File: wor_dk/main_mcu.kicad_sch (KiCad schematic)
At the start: 54 parts, among them J201 USB_A, J202 Prog, J203 u.FL, SW201 SW_Push, SW202 SW_Push, U201 nRF52840, Y201 32MHz, Y202 32.768kHz

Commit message: wor_dk: add top-level hierarchical sheets & update annotation
- import hierarchical sheet for main MCU
- import hierarchical sheet for transceiver MCU
- import hierarchical sheet for controller MCU
- update annotations for controller MCU
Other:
- title: MCU -> Main MCU

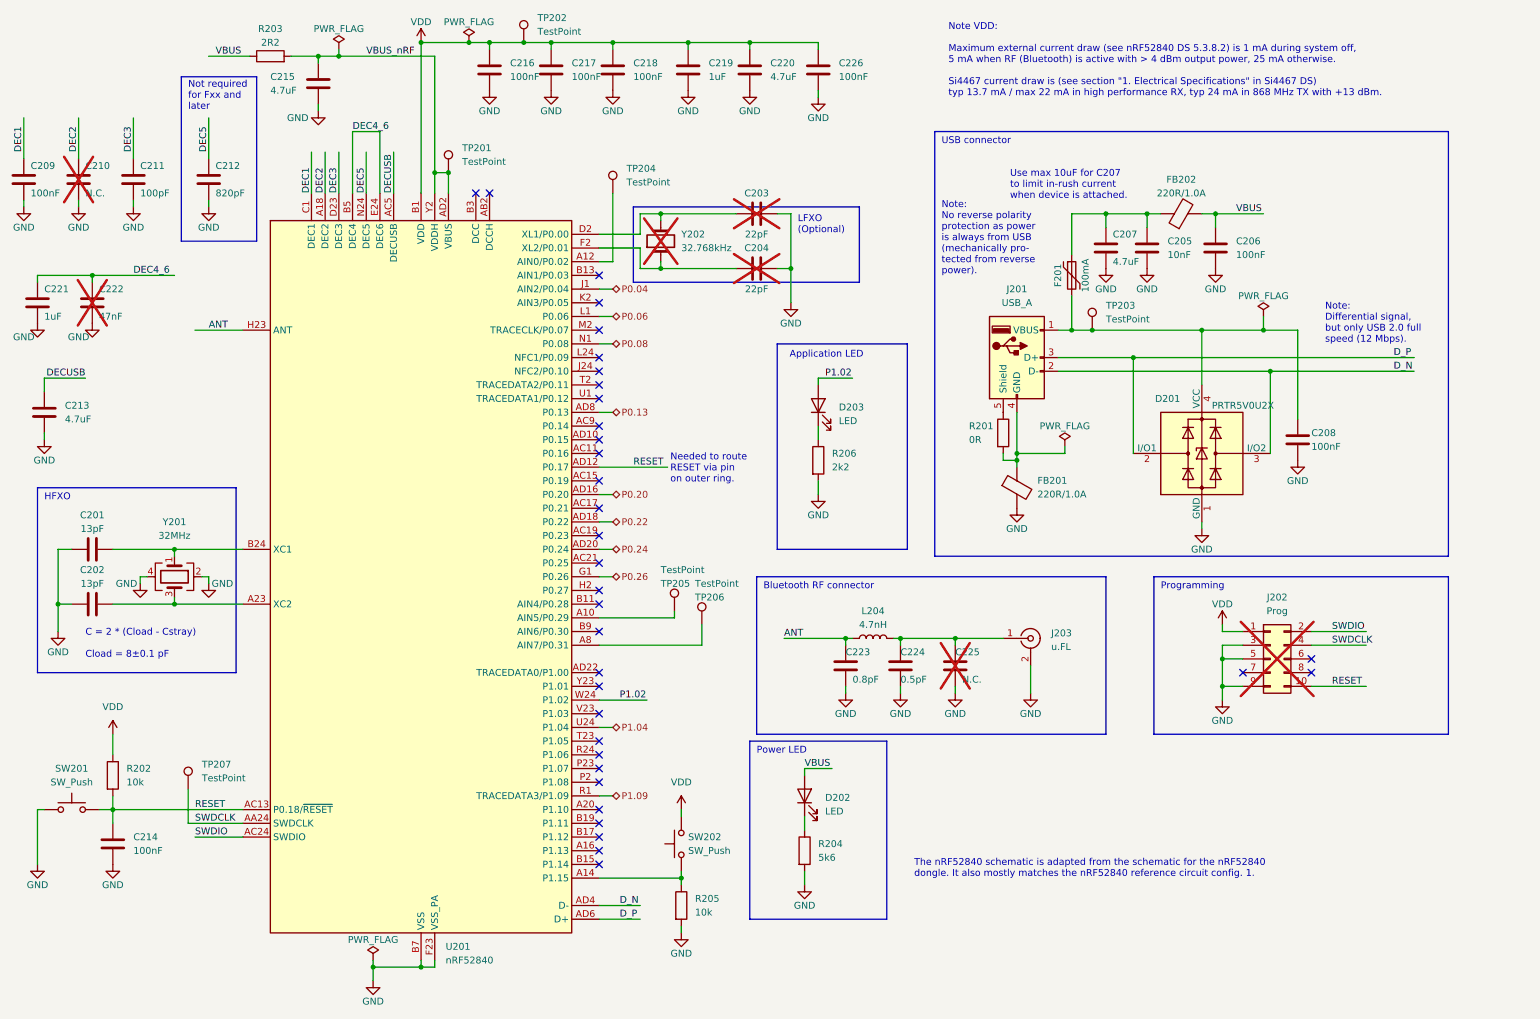
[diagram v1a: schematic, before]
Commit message: wor_dk: high-level adjustments for main MCU, transceiver & controller
Main MCU:
- populate 32 kHz crystal (remove DNP)
- populate programming connector (remove DNP)
- remove power LED
- remove application LED
- remove user button
- remove Bluetooth parts
- remove USB connector & parts

Transceiver:
- remove RX/TX LEDs

Controller MCU:
- populate programming connector (remove DNP)
- remove 32 kHz crystal & capacitors
- remove Bluetooth parts
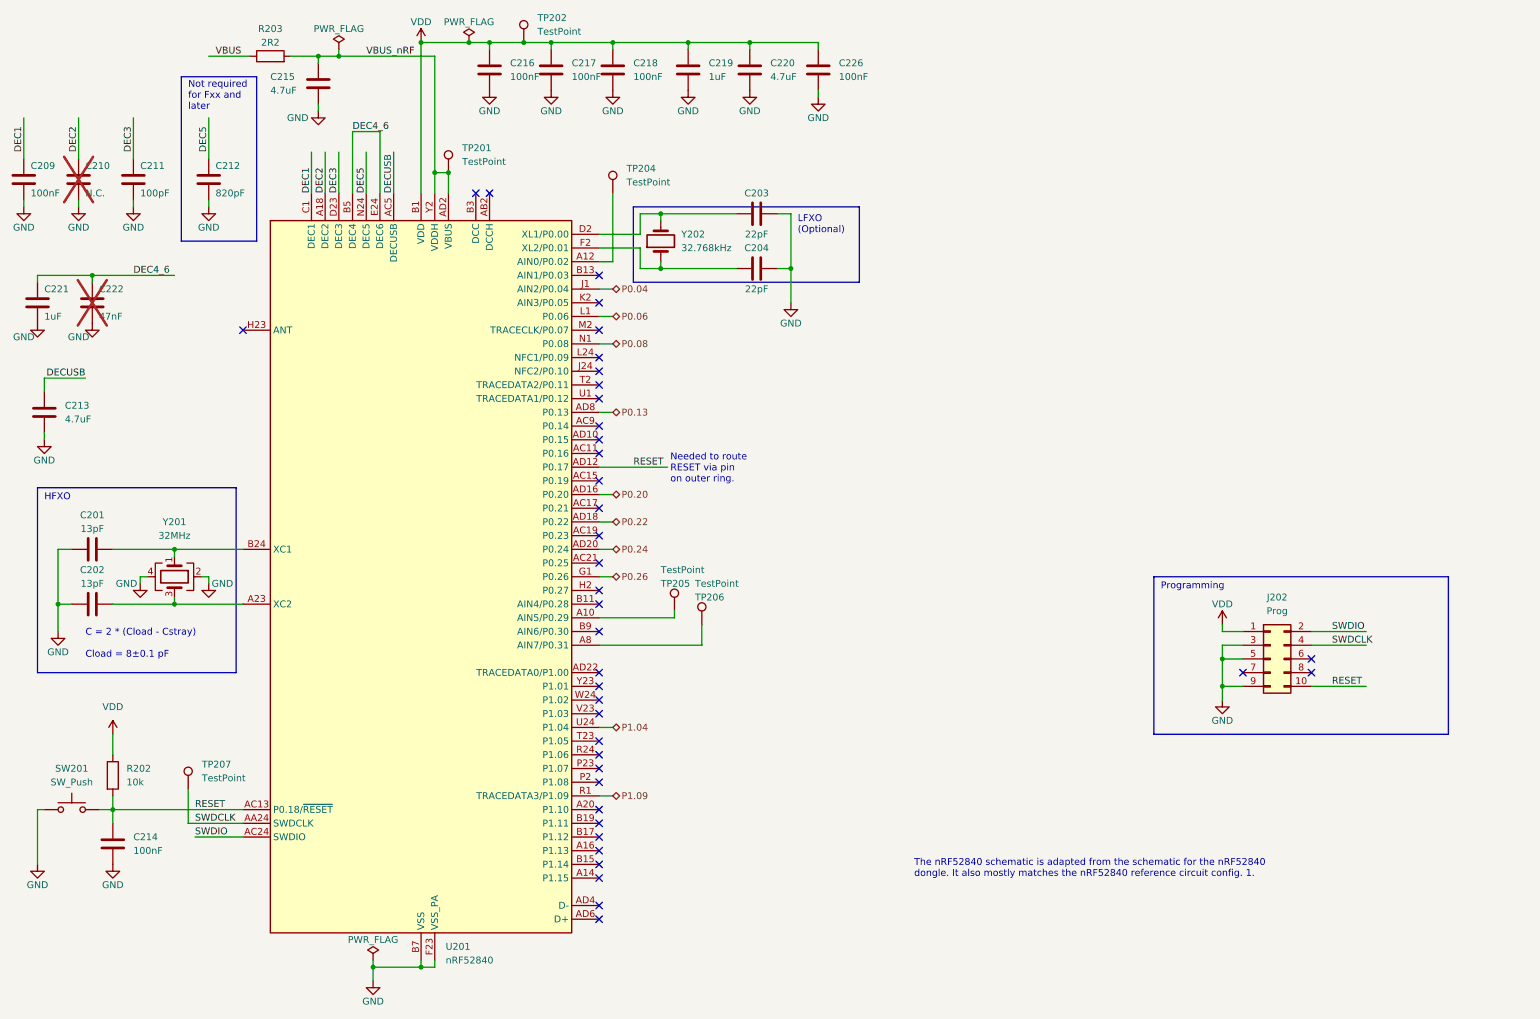
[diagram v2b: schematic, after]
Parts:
- removed C205: 10nF, Capacitor_SMD:C_0201_0603Metric, symbol Device:C
- removed C206, C208: 100nF, Capacitor_SMD:C_0201_0603Metric, symbol Device:C
- removed C207: 4.7uF, Capacitor_SMD:C_0402_1005Metric, symbol Device:C
- removed C223: 0.8pF, Capacitor_SMD:C_0201_0603Metric, symbol Device:C
- removed C224: 0.5pF, Capacitor_SMD:C_0201_0603Metric, symbol Device:C
- removed C225: N.C., Capacitor_SMD:C_0201_0603Metric, symbol Device:C
- removed D201: PRTR5V0U2X, Package_TO_SOT_SMD:SOT-143, symbol Power_Protection:PRTR5V0U2X
- removed D202, D203: LED, LED_SMD:LED_0805_2012Metric, symbol Device:LED
- removed F201: 100mA, Fuse:Fuse_0603_1608Metric, symbol Device:Polyfuse
- removed FB201, FB202: 220R/1.0A, Resistor_SMD:R_0402_1005Metric, symbol Device:FerriteBead
- removed J201: USB_A, Connector_USB:USB_A_CNCTech_1001-011-01101_Horizontal, symbol Connector:USB_A
- removed J203: u.FL, Connector_Coaxial:U.FL_Hirose_U.FL-R-SMT-1_Vertical, symbol Connector:Conn_Coaxial
- removed L204: 4.7nH, Inductor_SMD:L_0201_0603Metric, symbol Device:L
- removed R201: 0R, Resistor_SMD:R_0402_1005Metric, symbol Device:R
- removed R204: 5k6, Resistor_SMD:R_0402_1005Metric, symbol Device:R
- removed R205: 10k, Resistor_SMD:R_0402_1005Metric, symbol Device:R
- removed R206: 2k2, Resistor_SMD:R_0402_1005Metric, symbol Device:R
- removed SW202: SW_Push, Button_Switch_SMD:SW_SPST_PTS810, symbol Switch:SW_Push
- removed TP203: TestPoint, TestPoint:TestPoint_Pad_D1.0mm, symbol Connector:TestPoint
- C203, C204, Y202: now fitted; now in the parts list
- J202: now fitted
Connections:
- net ANT: no longer names the net of U201.H23 (ANT)
- net D_N: no longer names the net of U201.AD4 (D-)
- net D_P: no longer names the net of U201.AD6 (D+)
- net P1.02: no longer names the net of U201.W24 (P1.02)
- no-connect marks 34 -> 39
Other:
- note removed: "Application LED"
- note removed: "Bluetooth RF connector"
- note removed: "Note VDD: Maximum external current draw (see nRF52840 DS 5.3.8.2) is 1 mA during system off, 5 mA when RF (Bluetooth) is active with > 4 dBm output power, 25 mA otherwise. Si4467 current draw is (see section "1. Electrical Specifications" in Si4467 DS) typ 13.7 mA / max 22 mA in high performance RX, typ 24 mA in 868 MHz TX with +13 dBm."
- note removed: "Note: Differential signal, but only USB 2.0 full speed (12 Mbps)."
- note removed: "Note: No reverse polarity protection as power is always from USB (mechanically pro- tected from reverse power)."
- note removed: "Power LED"
- note removed: "USB connector"
- note removed: "Use max 10uF for C207 to limit in-rush current when device is attached."

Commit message: wor_dk: adapt main MCU power supply to externally powered
The main MCU now has support for enabling DC/DC converter for REG1 as
per reference circuit configuration no. 5.
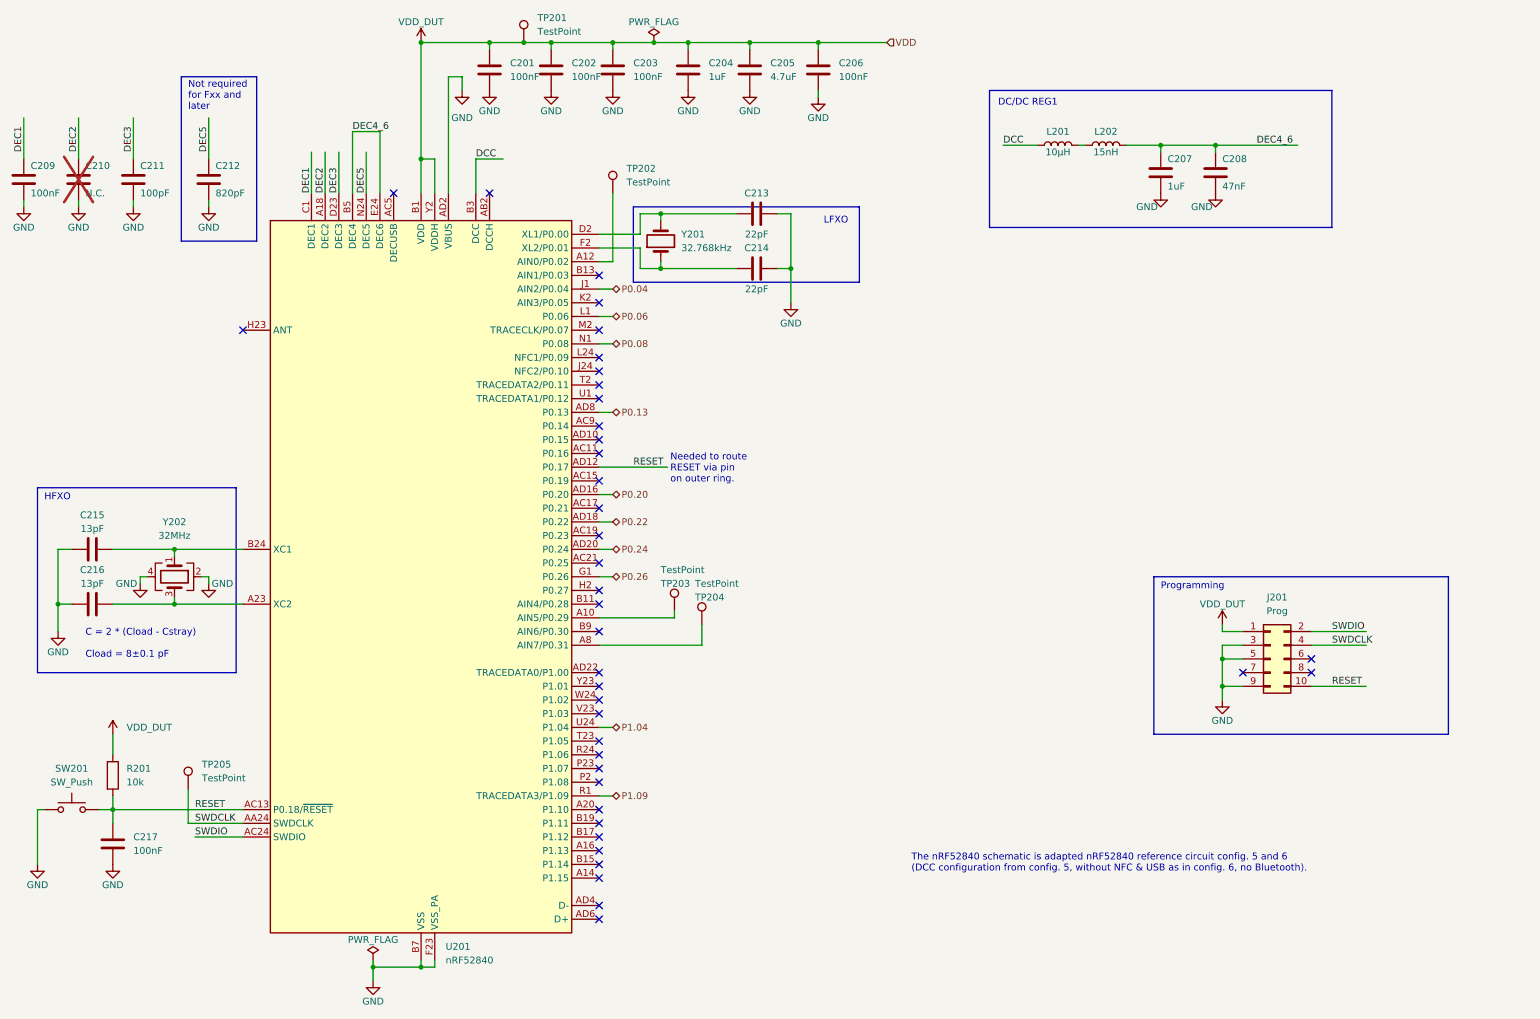
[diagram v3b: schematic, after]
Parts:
- removed C213: 4.7uF, Capacitor_SMD:C_0603_1608Metric, symbol Device:C
- removed C215: 4.7uF, Capacitor_SMD:C_0402_1005Metric, symbol Device:C
- removed C221: 1uF, Capacitor_SMD:C_0603_1608Metric, symbol Device:C
- removed C222: 47nF, Capacitor_SMD:C_0201_0603Metric, symbol Device:C
- removed R203: 2R2, Resistor_SMD:R_0201_0603Metric, symbol Device:R
- removed TP201: TestPoint, TestPoint:TestPoint_Pad_D1.0mm, symbol Connector:TestPoint
- added C207: 1uF, Resistor_SMD:R_0603_1608Metric, symbol Device:C
- added C208: 47nF, Resistor_SMD:R_0201_0603Metric, symbol Device:C
- added L201: 10μH, Inductor_SMD:L_0603_1608Metric, symbol Device:L
- added L202: 15nH, Inductor_SMD:L_0402_1005Metric, symbol Device:L
- renumbered C216 to C201, C217 to C202, C218 to C203, C219 to C204, C220 to C205, C226 to C206, C203 to C213, C204 to C214, C201 to C215, C202 to C216, C214 to C217, J202 to J201, R202 to R201, TP202 to TP201, TP204 to TP202, TP205 to TP203, TP206 to TP204, TP207 to TP205, Y202 to Y201, Y201 to Y202
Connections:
- net VDD is gone; now on net VDD_DUT: C201.1, C202.1, C203.1, C204.1, C205.1, C206.1, J201.1 (Pin_1), R201.1, TP201.1, U201.A22 (VDD), U201.AD14 (VDD), U201.AD23 (VDD), U201.B1 (VDD), U201.W1 (VDD)
- net DEC4_6: now also C207.1, C208.1, L202.2
- net GND: now also U201.AD2 (VBUS), C207.2, C208.2
- net DCC: now reaches U201.B3 (DCC)
- net DCC: now also L201.1
- net DECUSB: no longer names the net of U201.AC5 (DECUSB)
- net VBUS_nRF renamed VDD_DUT
- net VDD_DUT: no longer U201.AD2 (VBUS)
- new net: L201.2, L202.1
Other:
- note added: "DC/DC REG1"
- note added: "LFXO"
- note added: "The nRF52840 schematic is adapted nRF52840 reference circuit config. 5 and 6 (DCC configuration from config. 5, without NFC & USB as in config. 6, no Bluetooth)."
- note removed: "LFXO (Optional)"
- note removed: "The nRF52840 schematic is adapted from the schematic for the nRF52840 dongle. It also mostly matches the nRF52840 reference circuit config. 1."

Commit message: wor_dk: schematic: add multiplexers for programmer & GPIO
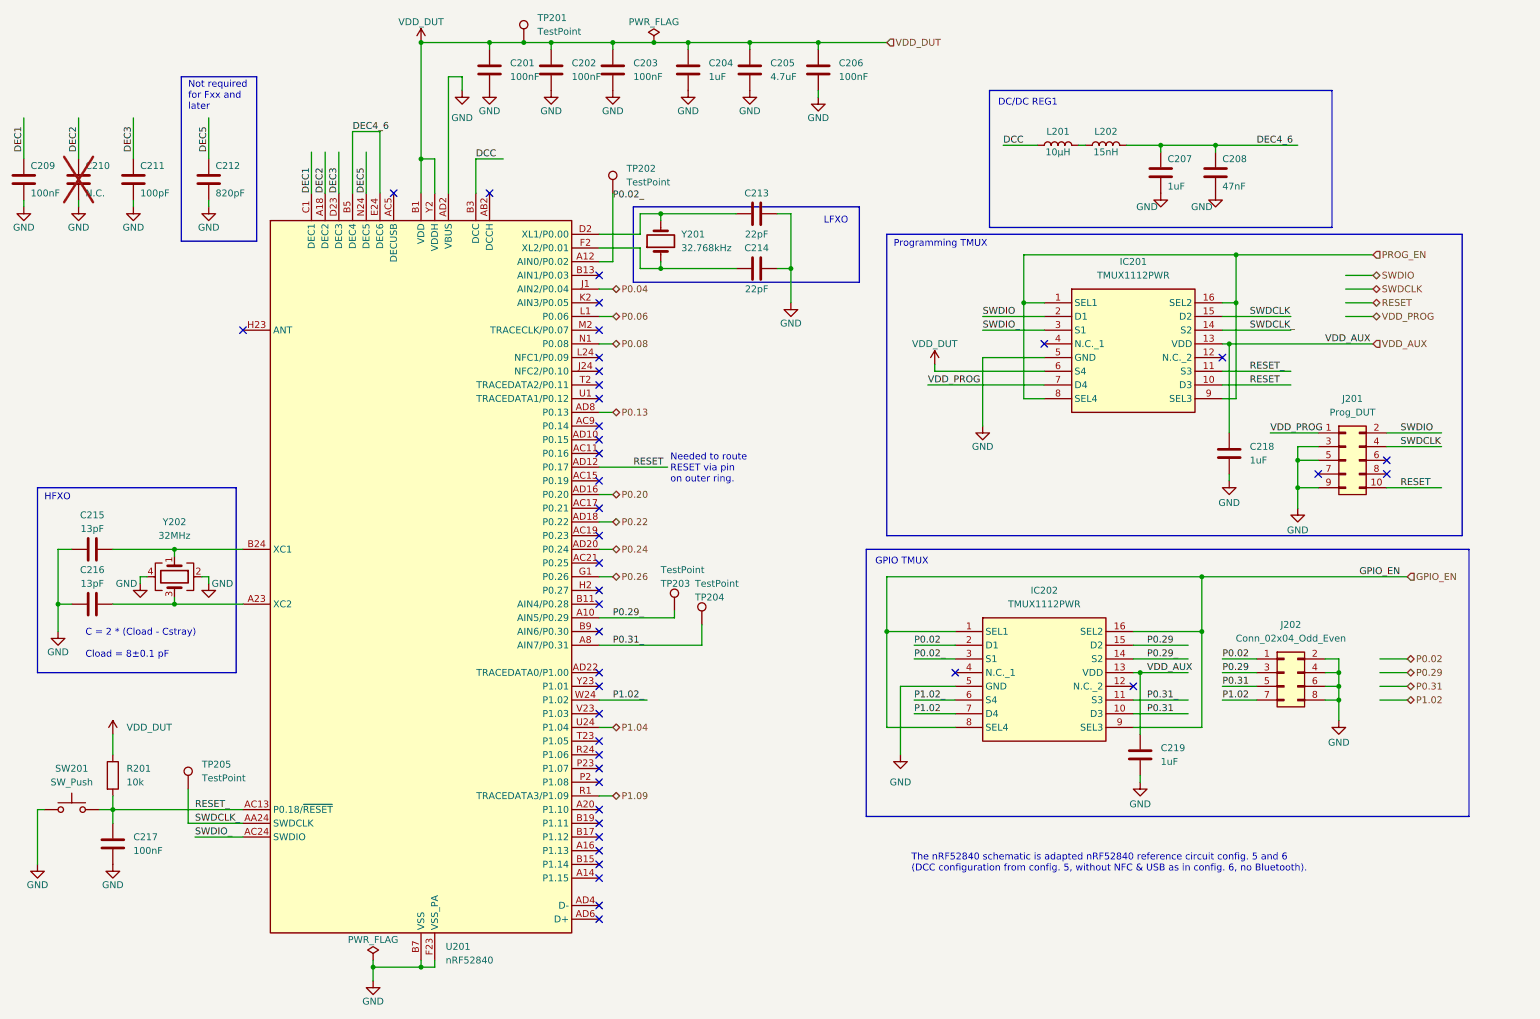
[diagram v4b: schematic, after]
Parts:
- added C218, C219: 1uF, Capacitor_SMD:C_0603_1608Metric, symbol Device:C
- added IC201, IC202: TMUX1112PWR, SOP65P640X120-16N, symbol TMUX1112PWR:TMUX1112PWR
- added J202: Conn_02x04_Odd_Even, symbol Connector_Generic:Conn_02x04_Odd_Even
- J201: value Prog -> Prog_DUT
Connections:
- net GND: now also C218.2, C219.2, IC201.5 (GND), IC202.5 (GND), J202.2 (Pin_2), J202.4 (Pin_4), J202.6 (Pin_6), J202.8 (Pin_8)
- net RESET: now also IC201.10 (D3); no longer C217.1, R201.2, SW201.2, U201.AC13 (P0.18/~{RESET})
- net SWDCLK: now also IC201.15 (D2); no longer TP205.1, U201.AA24 (SWDCLK)
- net SWDIO: now also IC201.2 (D1); no longer U201.AC24 (SWDIO)
- net VDD_DUT: now also IC201.6 (S4); no longer J201.1 (Pin_1)
- net P0.29_: now reaches TP203.1, U201.A10 (AIN5/P0.29)
- net P0.29_: now also IC202.14 (S2)
- net P0.02_: now reaches TP202.1, U201.A12 (AIN0/P0.02)
- net P0.02_: now also IC202.3 (S1)
- net P0.31_: now reaches TP204.1, U201.A8 (AIN7/P0.31)
- net P0.31_: now also IC202.11 (S3)
- net P1.02_: now reaches U201.W24 (P1.02)
- net P1.02_: now also IC202.6 (S4)
- new net GPIO_EN: IC202.1 (SEL1), IC202.16 (SEL2), IC202.8 (SEL4), IC202.9 (SEL3)
- new net P0.02: IC202.2 (D1), J202.1 (Pin_1)
- new net P0.29: IC202.15 (D2), J202.3 (Pin_3)
- new net P0.31: IC202.10 (D3), J202.5 (Pin_5)
- new net P1.02: IC202.7 (D4), J202.7 (Pin_7)
- new net PROG_EN: IC201.1 (SEL1), IC201.16 (SEL2), IC201.8 (SEL4), IC201.9 (SEL3)
- new net RESET_: C217.1, IC201.11 (S3), R201.2, SW201.2, U201.AC13 (P0.18/~{RESET})
- new net SWDCLK_: IC201.14 (S2), TP205.1, U201.AA24 (SWDCLK)
- new net SWDIO_: IC201.3 (S1), U201.AC24 (SWDIO)
- new net VDD_AUX: C218.1, C219.1, IC201.13 (VDD), IC202.13 (VDD)
- new net VDD_PROG: IC201.7 (D4), J201.1 (Pin_1)
- no-connect marks 39 -> 42
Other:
- note added: "GPIO TMUX"
- note added: "Programming TMUX"
- note removed: "Programming"
